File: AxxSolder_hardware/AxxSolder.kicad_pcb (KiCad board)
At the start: 2 copper layers, 39 x 82.5 mm, 145 parts, among them IC1 TLV76733DRVR, IC2 OPA2387DSGT, IC3 LMR54406DBVR, IC4 STM32G431CBT6, IC5 TPD4E1U06DBVR, IC6 STUSB4500QTR, IC7 MAX16171ATA_VY+T, IC8 LTC4440AHMS8E, IC9 INA281A5QDBVRQ1, J1 USB4110-GF-A, J2 691243110008, J3 TSW-102-07-T-S, J4 61300611821, J5 TSW-102-07-T-S, J6 TSW-102-07-T-S, J7 TSW-108-07-T-S, Q1 STL9P3LLH6, Q2 STL10N3LLH5, Q3 2N7002NXAKR, U2 PEC11J-9215F-S0015, U3 BSC014N04LS

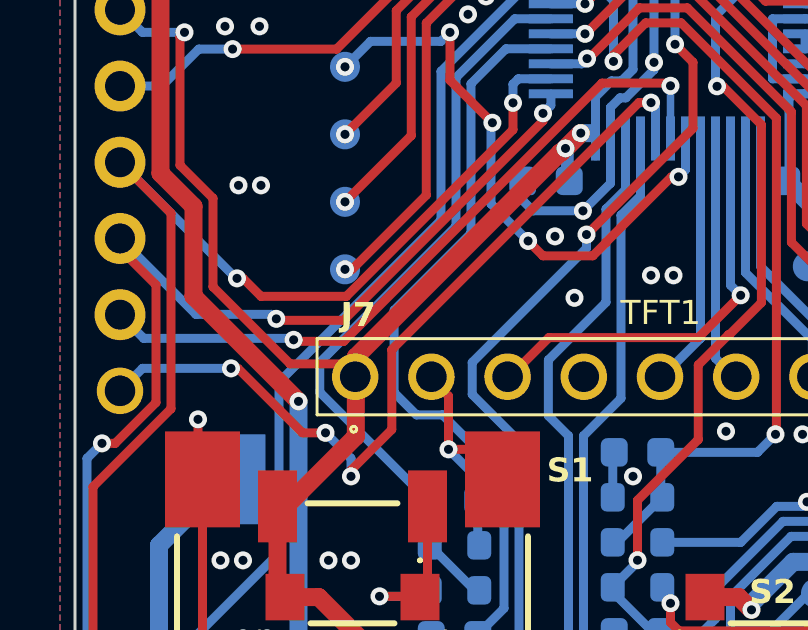
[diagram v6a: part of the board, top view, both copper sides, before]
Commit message: Update footprint name of STL9P3LLH6 to be correct
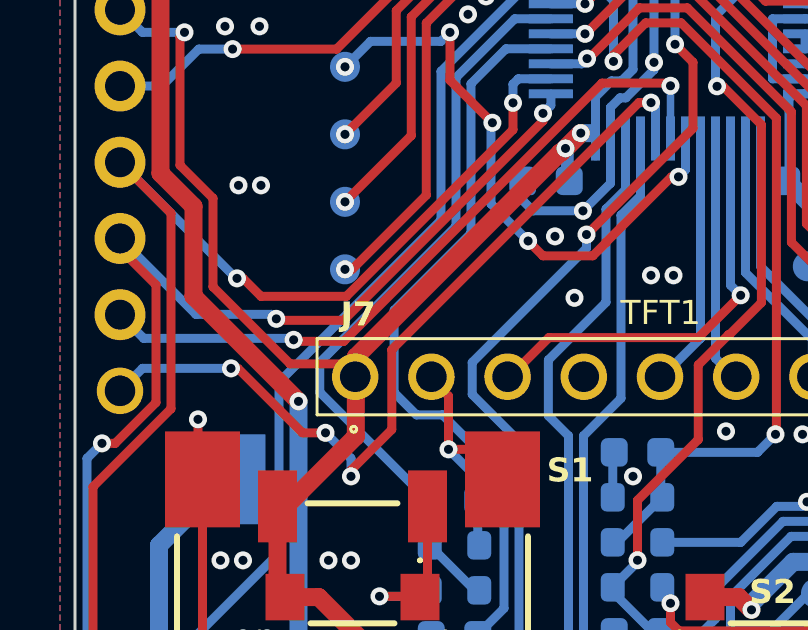
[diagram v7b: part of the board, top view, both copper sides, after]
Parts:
- J2: value 691243110008 -> 691243110009
- Q1: footprint footprints:STL20N6F7 -> footprints:STL9P3LLH6
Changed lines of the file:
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@@
     (property "ki_description" "8 Position, Single Row, Classic PCB Header Strips, 0.100&quot; pitch")
     (attr through_hole)
-    (fp_text reference "J7" (at 0.1 -2.06) (layer "F.SilkS")
+    (fp_text reference "J7" (at 0.1 -2.08) (layer "F.SilkS")
         (effects (font (size 0.8 0.8) (thickness 0.15) bold))
     )
@@
         (effects (font (size 0.8 0.8) (thickness 0.15)) (justify mirror))
     )
-    (fp_text value "691243110008" (at -12.25 0.15 90) (layer "B.SilkS") hide
+    (fp_text value "691243110009" (at -12.25 0.15 90) (layer "B.SilkS") hide
         (effects (font (size 0.8 0.8) (thickness 0.15)) (justify mirror))
     )
@@
     (property "Sheetname" "")
     (property "ki_description" "CONN USB 2.0 TYPE-C R/A SMT")
-    (fp_text reference "J1" (at 5.4 -2.95) (layer "B.SilkS")
+    (attr through_hole)
+    (fp_text reference "J1" (at 5.5 -2.8) (layer "B.SilkS")
         (effects (font (size 0.8 0.8) (thickness 0.15) bold) (justify mirror))
     )
@@
       (net 28 "/CC1") (pinfunction "1") (pintype "passive"))
   )
-  (footprint "footprints:STL20N6F7" (layer "B.Cu")
+  (footprint "footprints:STL9P3LLH6" (layer "B.Cu")
     (at 195 137.75 90)
     (descr "PowerFLAT™ 3.3x3.3")
@@
     (property "ki_description" "MOSFET P-channel -30 V, 12 mOhm typ., -9 A STripFET H6 Power MOSFET in a PowerFLAT 3.3 x 3.3 package")
     (attr smd)
-    (fp_text reference "Q1" (at 2.25 1.25 180) (layer "B.SilkS")
-        (effects (font (size 0.8 0.8) (thickness 0.15)) (justify mirror))
+    (fp_text reference "Q1" (at 2.25 1.25) (layer "B.SilkS")
+        (effects (font (size 0.8 0.8) (thickness 0.15) bold) (justify mirror))
     )
-    (fp_text value "STL9P3LLH6" (at 0 -0.2 90) (layer "B.SilkS") hide
-        (effects (font (size 0.8 0.8) (thickness 0.15)) (justify mirror))
+    (fp_text value "STL9P3LLH6" (at 0 -0.2 270) (layer "B.SilkS") hide
+        (effects (font (size 1.27 1.27) (thickness 0.254)) (justify mirror))
     )
-    (fp_text user "${REFERENCE}" (at 0 -0.2 90) (layer "B.Fab")
-        (effects (font (size 0.8 0.8) (thickness 0.15)) (justify mirror))
+    (fp_text user "${REFERENCE}" (at 0 -0.2 270) (layer "B.Fab")
+        (effects (font (size 1.27 1.27) (thickness 0.254)) (justify mirror))
     )
     (fp_line (start -1.575 -1.5) (end -1.4 -1.5)
@@
     (property "ki_description" "EEV, Aluminum, Aluminum Electrolytic, 220 uF, 20%, 35 VDC, -55/+105C, 105C, -55C, 105C, 2,000 Hrs, 12 % , 160 mOhms, 0.42, 77 uA, 2, 3, 8mm, 10.2mm, 500")
     (attr smd)
-    (fp_text reference "C37" (at -4.85 4.8) (layer "B.SilkS")
+    (fp_text reference "C37" (at -4.65 5.05) (layer "B.SilkS")
         (effects (font (size 0.8 0.8) (thickness 0.15) bold) (justify mirror))
     )
@@
     (property "ki_description" "Switching Voltage Regulators SIMPLE SWITCHER power converter 4.5-V to 36-V, 0.6-A, synchronous buck with 80-uA IQ")
     (attr smd)
-    (fp_text reference "IC3" (at 0 -2.25 180) (layer "B.SilkS")
+    (fp_text reference "IC3" (at 0 -2.35 180) (layer "B.SilkS")
         (effects (font (size 0.8 0.8) (thickness 0.15) bold) (justify mirror))
     )
@@
     (property "ki_description" "Quad High Speed ESD Protection SOT-23-6 Texas Instruments TPD4E1U06DBVR Quad Uni-Directional ESD Protection Array, 45W peak, 6-Pin SOT-23")
     (attr smd)
-    (fp_text reference "IC5" (at 0 2.25) (layer "B.SilkS")
+    (fp_text reference "IC5" (at 0 2.4) (layer "B.SilkS")
         (effects (font (size 0.8 0.8) (thickness 0.15) bold) (justify mirror))
     )
@@
     (pts (xy 161 67.5) (xy 200 67.5))
     (height -2.5)
-    (gr_text "39,0000 mm" (at 180.5 63.85) (layer "User.4")
+    (gr_text "39.0000 mm" (at 180.5 63.85) (layer "User.4")
       (effects (font (size 1 1) (thickness 0.15)))
     )
@@
     (pts (xy 164 67.5) (xy 164 150))
     (height 6.499999)
-    (gr_text "82,5000 mm" (at 156.350001 108.75 90) (layer "User.4")
+    (gr_text "82.5000 mm" (at 156.350001 108.75 90) (layer "User.4")
       (effects (font (size 1 1) (thickness 0.15)))
     )
